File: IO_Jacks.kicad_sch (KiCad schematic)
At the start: 45 parts, among them J10 3085_MiniJack_Thonk_Vert, J11 3085_MiniJack_Thonk_Vert, J12 3085_MiniJack_Thonk_Vert, J4 CV_OFFSET, J5 3085_MiniJack_Thonk_Vert, J6 3085_MiniJack_Thonk_Vert, J7 3085_MiniJack_Thonk_Vert, J8 3085_MiniJack_Thonk_Vert, J9 3085_MiniJack_Thonk_Vert, U5 4014_Voltage_Reference_5V_SOT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, U6 4001_MCP48FEB24_DAC, U7 3099_TL074CPW_SMD, U8 3099_TL074CPW_SMD

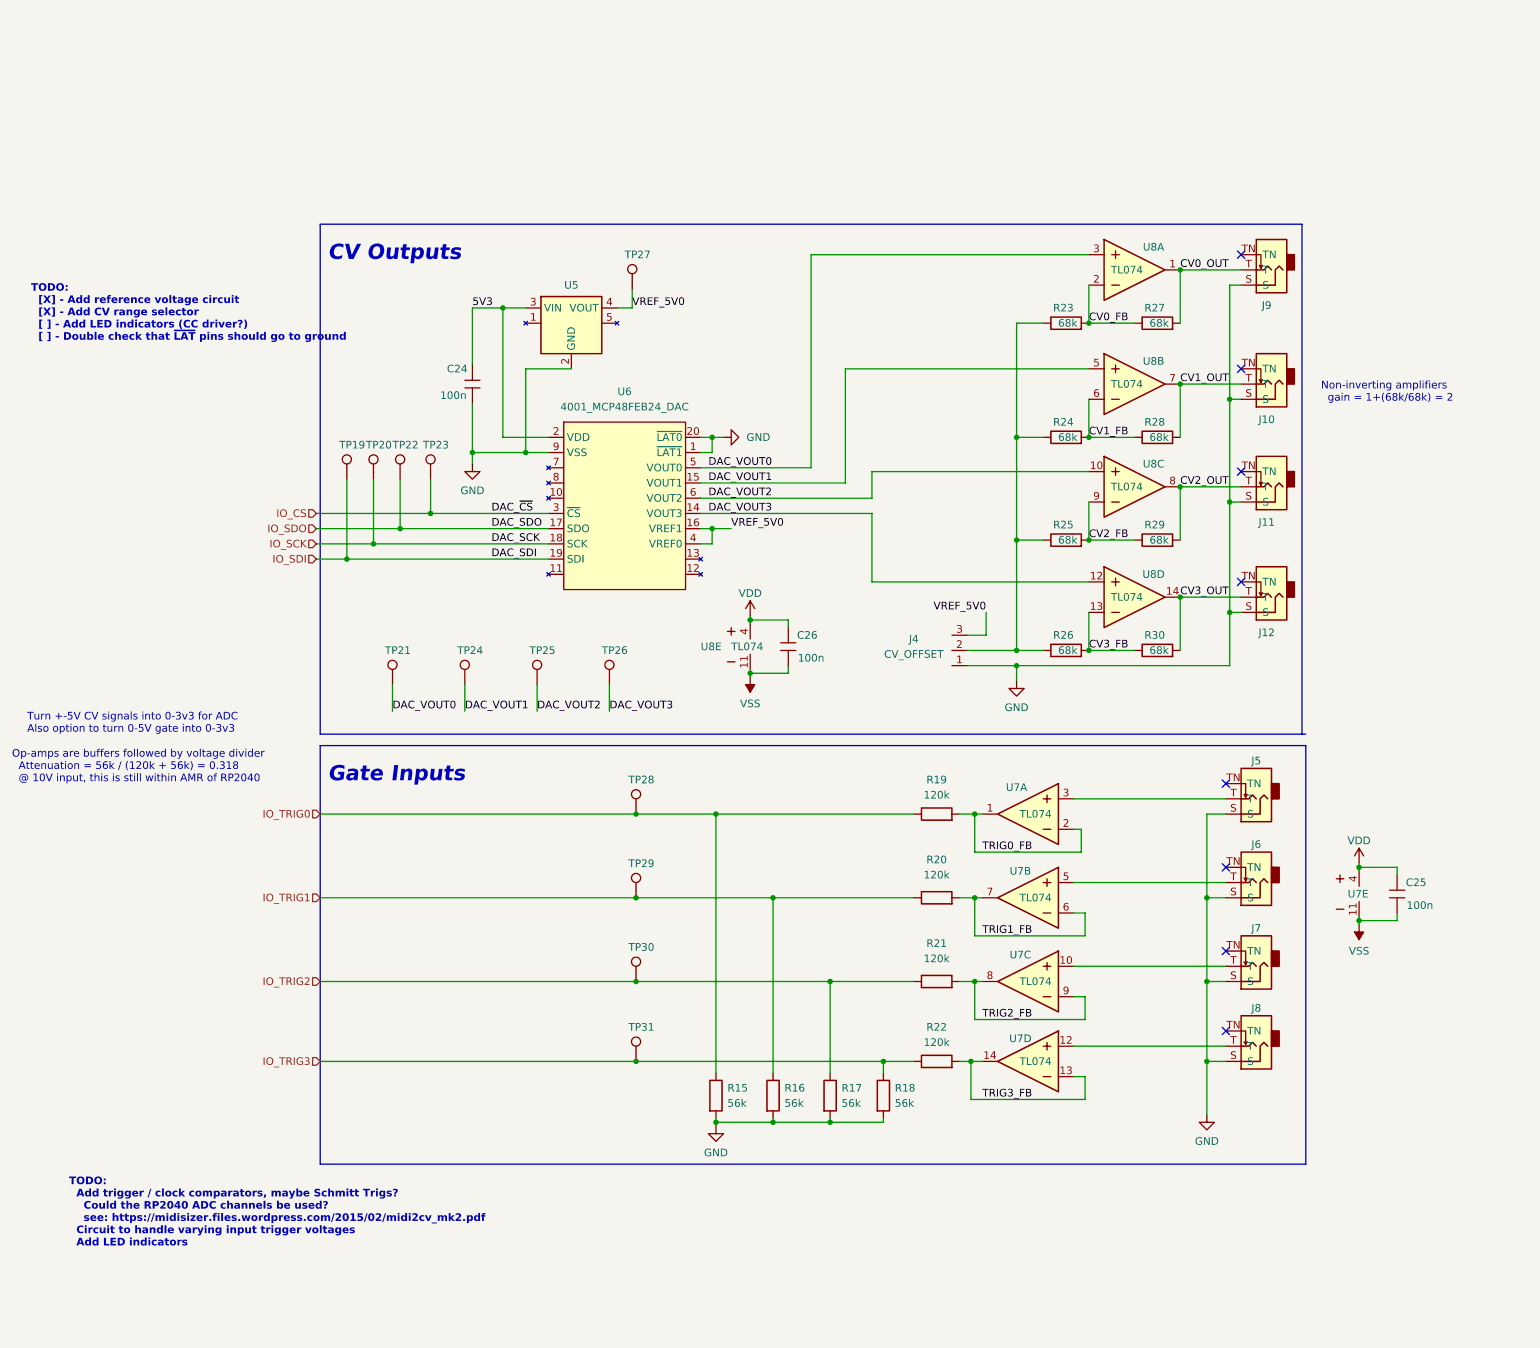
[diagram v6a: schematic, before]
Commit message: gots most components placed nicely, added 4027 for MIDI, still to finish
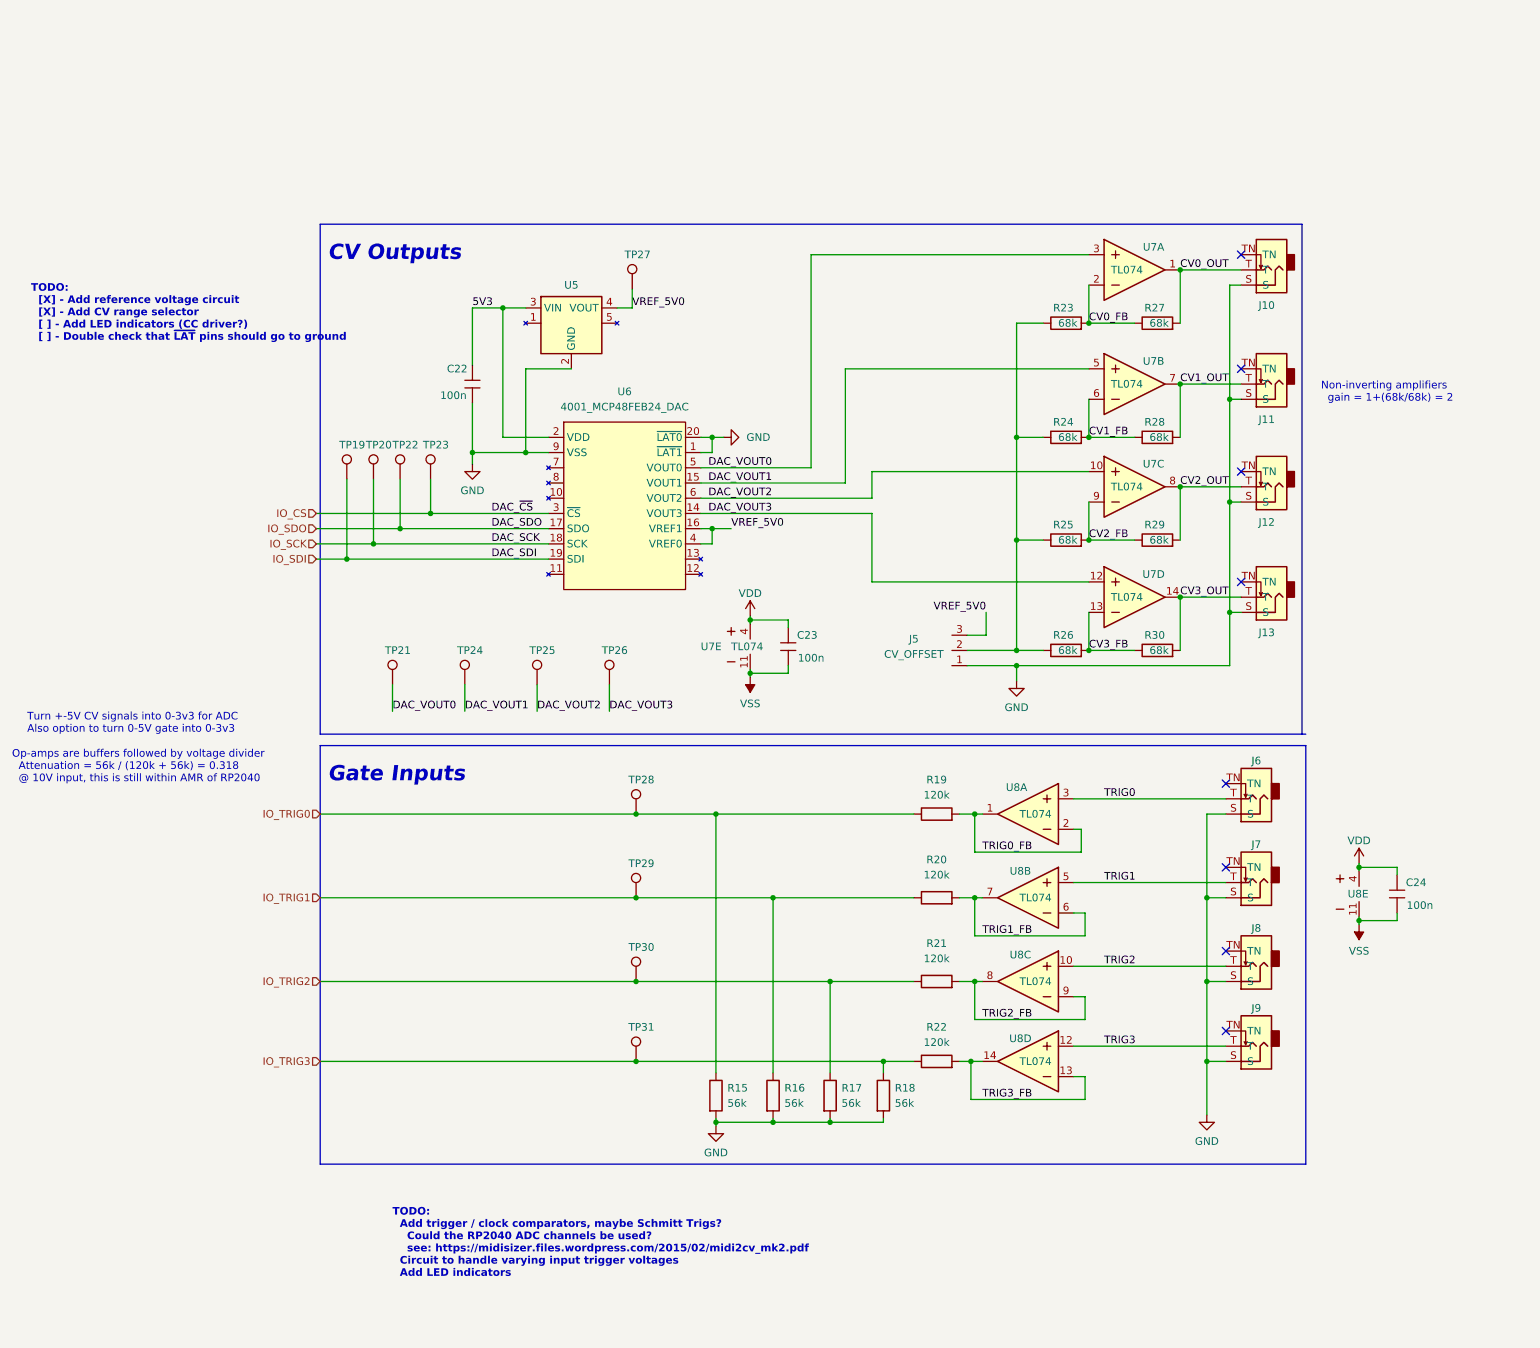
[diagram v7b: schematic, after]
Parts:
- renumbered C24 to C22, C26 to C23, C25 to C24, J9 to J10, J10 to J11, J11 to J12, J12 to J13, J4 to J5, J5 to J6, J6 to J7, J7 to J8, J8 to J9, U8 to U7, U7 to U8
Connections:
- net TRIG2: now reaches J8.T, U8.10 (3IN+)
- net TRIG1: now reaches J7.T, U8.5 (2IN+)
- net TRIG0: now reaches J6.T, U8.3 (1IN+)
- net TRIG3: now reaches J9.T, U8.12 (4IN+)

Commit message: Made minor tweaks, started routing of board
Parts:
- J5: SPN (none) -> 3046
- U6: SPN (none) -> 4001
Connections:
- net CVx_REF: now reaches J5.2, R23.1, R24.1, R25.1, R26.1
- net 5V3 renamed IO_5V3
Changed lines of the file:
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@@
   (junction (at 99.06 52.07) (diameter 0) (color 0 0 0 0)
+  )
+  (junction (at 90.17 27.94) (diameter 0) (color 0 0 0 0)
   )
   (junction (at 208.28 57.785) (diameter 0) (color 0 0 0 0)
@@
     (stroke (width 0) (type default) (color 0 0 0 0))
   )
+  (wire (pts (xy 79.375 43.815) (xy 79.375 27.94))
+    (stroke (width 0) (type default) (color 0 0 0 0))
+  )
   (wire (pts (xy 146.685 54.61) (xy 128.27 54.61))
     (stroke (width 0) (type default) (color 0 0 0 0))
@@
     (stroke (width 0) (type default) (color 0 0 0 0))
   )
+  (wire (pts (xy 64.77 43.815) (xy 79.375 43.815))
+    (stroke (width 0) (type default) (color 0 0 0 0))
+  )
   (wire (pts (xy 238.125 120.65) (xy 238.125 121.285))
     (stroke (width 0) (type default) (color 0 0 0 0))
@@
   )
   (wire (pts (xy 238.125 121.285) (xy 238.125 121.92))
+    (stroke (width 0) (type default) (color 0 0 0 0))
+  )
+  (wire (pts (xy 79.375 27.94) (xy 90.17 27.94))
     (stroke (width 0) (type default) (color 0 0 0 0))
   )
@@
     (effects (font (size 1.27 1.27)) (justify left bottom))
   )
+  (label "CVx_REF" (at 180.975 85.09 90)
+    (effects (font (size 1.27 1.27)) (justify left bottom))
+  )
   (hierarchical_label "IO_TRIG2" (shape input) (at 64.77 140.335 180)
+    (effects (font (size 1.27 1.27)) (justify right))
+  )
+  (hierarchical_label "IO_5V3" (shape input) (at 64.77 43.815 180)
     (effects (font (size 1.27 1.27)) (justify right))
   )
@@
     )
     (property "Datasheet" "http://ww1.microchip.com/downloads/en/DeviceDoc/MCP48FXBX4-8-Family-Data-Sheet-DS20006362A.pdf" (id 3) (at 115.57 59.69 0)
+      (effects (font (size 1.27 1.27)) hide)
+    )
+    (property "SPN" "4001" (id 4) (at 115.57 83.82 0)
       (effects (font (size 1.27 1.27)) hide)
     )
@@
       (effects (font (size 1.27 1.27)) hide)
     )
+    (property "SPN" "3046" (id 4) (at 171.45 80.01 0))
     (pin "1")
     (pin "2")
